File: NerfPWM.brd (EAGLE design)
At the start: 50.8 x 25.4 mm, 37 parts, among them IC1 MEGA48/88/168-AU

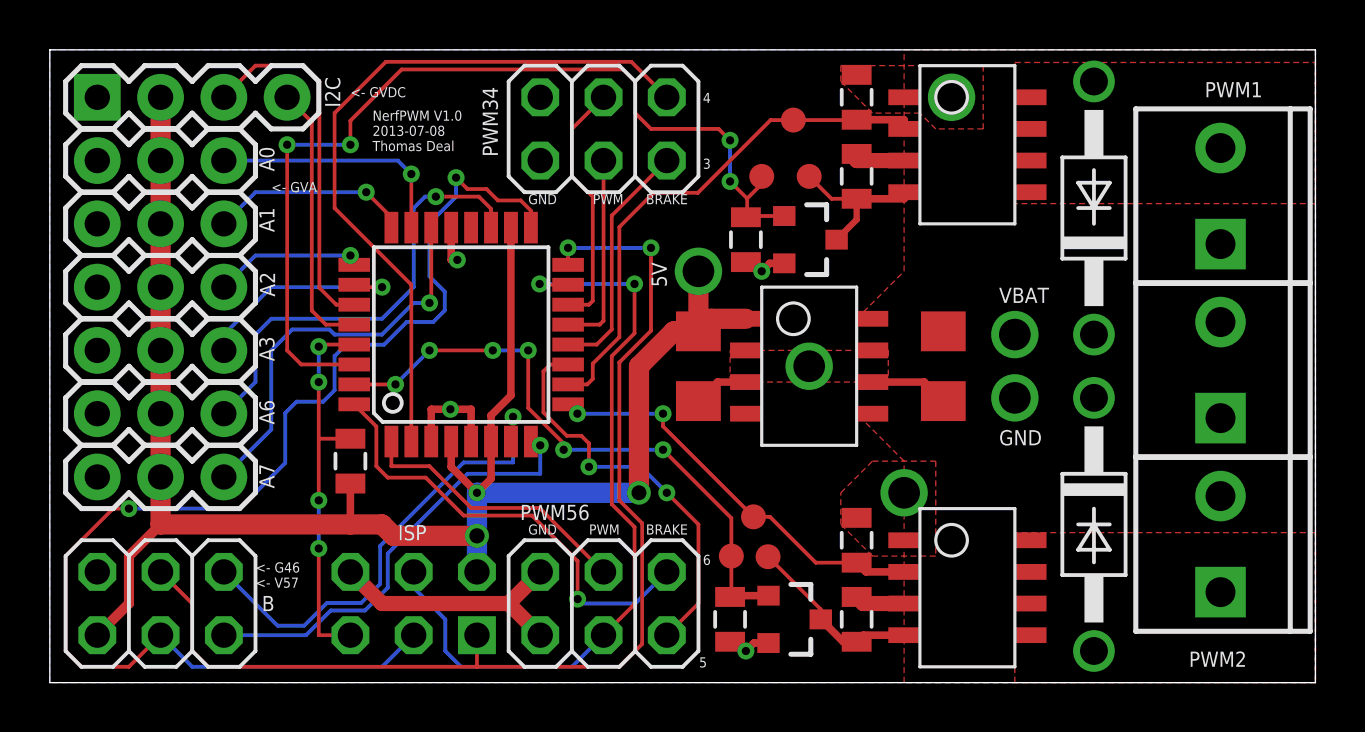
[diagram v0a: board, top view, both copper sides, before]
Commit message: Changed ISP header.
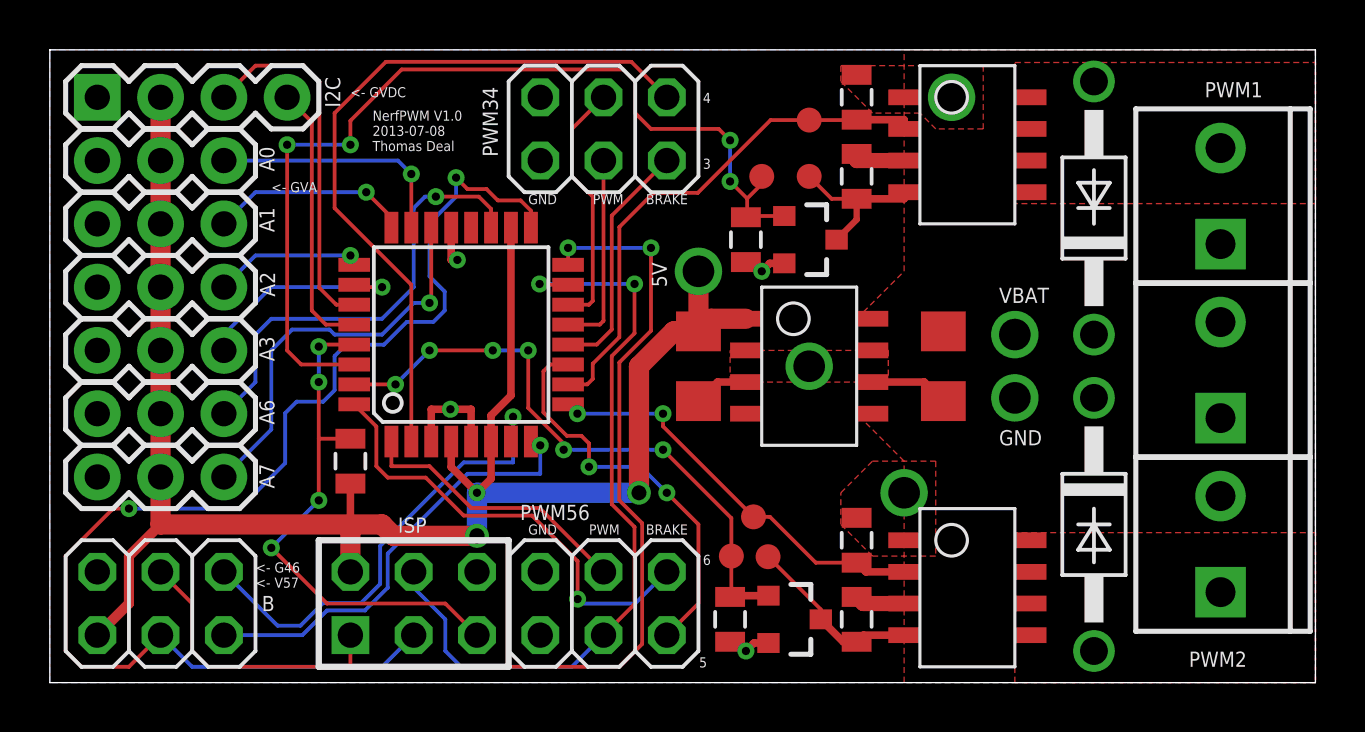
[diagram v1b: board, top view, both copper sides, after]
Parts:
- JP1: value AVR-ISP-6R -> AVR-ISP-6; device custom:AVR-ISP-6R -> custom:AVR-ISP-6
- moved PWM1 0.64 mm to (30.5, 22.6)
- flipped JP1 to the top
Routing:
- net GND: track 25.2 -> 14.8 mm
- net RESET: track 15.6 -> 21.3 mm
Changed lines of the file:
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@@
 <text x="26.0604" y="0.6096" size="0.4064" layer="21">5</text>
 <text x="26.2128" y="4.7244" size="0.4064" layer="21">6</text>
-<text x="13.97" y="5.715" size="0.6096" layer="21">ISP</text>
+<text x="13.97" y="6.0198" size="0.6096" layer="21">ISP</text>
 <text x="8.89" y="19.685" size="0.4064" layer="21">&lt;- GVA</text>
 <text x="12.065" y="23.495" size="0.4064" layer="21">&lt;- GVDC</text>
@@
 <attribute name="VALUE" x="29.6545" y="3.556" size="0.4064" layer="27" rot="R270"/>
 </element>
-<element name="JP1" library="custom" package="AVR-ISP-6R" value="AVR-ISP-6R" x="14.605" y="3.175" smashed="yes" rot="MR0"/>
+<element name="JP1" library="custom" package="AVR-ISP-6" value="AVR-ISP-6" x="14.605" y="3.175" smashed="yes"/>
 <element name="I2C" library="SparkFun" package="1X04" value="" x="1.905" y="23.495" smashed="yes">
 <attribute name="NAME" x="11.049" y="24.3078" size="0.6096" layer="21" ratio="10" rot="R270"/>
@@
 <attribute name="TP_SIGNAL_NAME" value="" x="28.2448" y="4.7498" size="1" layer="37"/>
 </element>
-<element name="PWM1" library="testpad" package="TP10R" value="TPTP10R" x="29.845" y="22.5806" smashed="yes">
-<attribute name="TP_SIGNAL_NAME" value="" x="29.845" y="20.6756" size="1" layer="37"/>
+<element name="PWM1" library="testpad" package="TP10R" value="TPTP10R" x="30.48" y="22.5806" smashed="yes">
+<attribute name="TP_SIGNAL_NAME" value="" x="30.48" y="20.6756" size="1" layer="37"/>
 </element>
 <element name="BRAKE1" library="testpad" package="TP10R" value="TPTP10R" x="28.575" y="20.32" smashed="yes">
@@
 <wire x1="27.305" y1="1.64" x2="27.57" y2="1.64" width="0.3048" layer="1"/>
 <wire x1="27.57" y1="1.64" x2="27.94" y2="1.27" width="0.3048" layer="1"/>
-<wire x1="19.685" y1="4.445" x2="18.415" y2="3.175" width="0.6096" layer="1"/>
-<wire x1="18.415" y1="3.175" x2="19.685" y2="1.905" width="0.6096" layer="1"/>
-<wire x1="18.415" y1="3.175" x2="13.335" y2="3.175" width="0.6096" layer="1"/>
-<wire x1="13.335" y1="3.175" x2="12.065" y2="4.445" width="0.6096" layer="1"/>
 <via x="38.735" y="11.43" extent="1-16" drill="1.27"/>
 </signal>
@@
 <wire x1="26.035" y1="14.1" x2="26.54" y2="14.605" width="0.8128" layer="1"/>
 <wire x1="26.54" y1="14.605" x2="27.94" y2="14.605" width="0.8128" layer="1"/>
-<wire x1="17.145" y1="4.445" x2="17.145" y2="5.8928" width="0.8128" layer="16"/>
 <via x="17.145" y="5.8928" extent="1-16" drill="0.6096"/>
 <wire x1="1.905" y1="1.905" x2="3.175" y2="3.175" width="0.4064" layer="1"/>
@@
 <via x="26.035" y="16.51" extent="1-16" drill="1.27"/>
 <wire x1="26.035" y1="16.51" x2="26.035" y2="14.1" width="0.8128" layer="1"/>
+<wire x1="12.065" y1="6.35" x2="12.065" y2="4.445" width="0.8128" layer="1"/>
 </signal>
 <signal name="VMOT1" class="3">
@@
 <contactref element="PWM1" pad="TP"/>
 <wire x1="32.385" y1="22.595" x2="32.3706" y2="22.5806" width="0.1524" layer="1"/>
-<wire x1="32.3706" y1="22.5806" x2="29.845" y2="22.5806" width="0.1524" layer="1"/>
-<wire x1="29.845" y1="22.5806" x2="28.9306" y2="22.5806" width="0.1524" layer="1"/>
+<wire x1="32.3706" y1="22.5806" x2="30.48" y2="22.5806" width="0.1524" layer="1"/>
+<wire x1="30.48" y1="22.5806" x2="28.9306" y2="22.5806" width="0.1524" layer="1"/>
 </signal>
 <signal name="BRAKE1">
@@
 <wire x1="4.445" y1="1.905" x2="5.715" y2="0.635" width="0.1524" layer="16"/>
 <wire x1="5.715" y1="0.635" x2="13.335" y2="0.635" width="0.1524" layer="16"/>
-<wire x1="13.335" y1="0.635" x2="14.605" y2="1.905" width="0.1524" layer="16"/>
 <wire x1="19.31" y1="18.2626" x2="19.31" y2="18.9424" width="0.1524" layer="1"/>
 <wire x1="19.31" y1="18.9424" x2="18.8976" y2="19.3548" width="0.1524" layer="1"/>
@@
 <wire x1="1.27" y1="0.635" x2="3.175" y2="0.635" width="0.1524" layer="1"/>
 <wire x1="3.175" y1="0.635" x2="4.445" y2="1.905" width="0.1524" layer="1"/>
+<wire x1="14.605" y1="1.905" x2="13.335" y2="0.635" width="0.1524" layer="16"/>
 </signal>
 <signal name="PWM5">
@@
 <contactref element="IC1" pad="15"/>
 <contactref element="PWM56" pad="3"/>
-<wire x1="14.605" y1="4.445" x2="14.605" y2="3.81" width="0.1524" layer="16"/>
-<wire x1="14.605" y1="3.81" x2="15.875" y2="2.54" width="0.1524" layer="16"/>
-<wire x1="15.875" y1="2.54" x2="15.875" y2="1.27" width="0.1524" layer="16"/>
-<wire x1="15.875" y1="1.27" x2="16.51" y2="0.635" width="0.1524" layer="16"/>
 <wire x1="16.51" y1="0.635" x2="20.955" y2="0.635" width="0.1524" layer="16"/>
 <wire x1="20.955" y1="0.635" x2="22.225" y2="1.905" width="0.1524" layer="16"/>
@@
 <wire x1="23.4696" y1="6.2484" x2="23.4696" y2="3.1496" width="0.1524" layer="1"/>
 <wire x1="23.4696" y1="3.1496" x2="22.225" y2="1.905" width="0.1524" layer="1"/>
+<wire x1="14.605" y1="4.445" x2="14.605" y2="3.81" width="0.1524" layer="16"/>
+<wire x1="14.605" y1="3.81" x2="15.875" y2="2.54" width="0.1524" layer="16"/>
+<wire x1="15.875" y1="2.54" x2="15.875" y2="1.27" width="0.1524" layer="16"/>
+<wire x1="15.875" y1="1.27" x2="16.51" y2="0.635" width="0.1524" layer="16"/>
 </signal>
 <signal name="B4">
@@
 <wire x1="5.715" y1="3.175" x2="5.715" y2="1.27" width="0.1524" layer="1"/>
 <wire x1="5.715" y1="1.27" x2="6.35" y2="0.635" width="0.1524" layer="1"/>
-<wire x1="6.35" y1="0.635" x2="17.145" y2="0.635" width="0.1524" layer="1"/>
-<wire x1="17.145" y1="0.635" x2="22.86" y2="0.635" width="0.1524" layer="1"/>
+<wire x1="6.35" y1="0.635" x2="12.065" y2="0.635" width="0.1524" layer="1"/>
+<wire x1="12.065" y1="0.635" x2="22.86" y2="0.635" width="0.1524" layer="1"/>
 <wire x1="22.86" y1="7.3152" x2="22.86" y2="12.8524" width="0.1524" layer="1"/>
 <wire x1="22.86" y1="12.8524" x2="24.13" y2="14.1224" width="0.1524" layer="1"/>
@@
 <wire x1="23.7744" y1="6.4008" x2="23.7744" y2="1.5494" width="0.1524" layer="1"/>
 <wire x1="23.7744" y1="1.5494" x2="22.86" y2="0.635" width="0.1524" layer="1"/>
-<wire x1="17.145" y1="1.905" x2="17.145" y2="0.635" width="0.1524" layer="1"/>
+<wire x1="12.065" y1="1.905" x2="12.065" y2="0.635" width="0.1524" layer="1"/>
 </signal>
 <signal name="RESET">
@@
 <wire x1="10.795" y1="12.065" x2="10.795" y2="9.79" width="0.1524" layer="1"/>
 <wire x1="10.795" y1="9.79" x2="12.065" y2="9.79" width="0.1524" layer="1"/>
-<wire x1="12.065" y1="1.905" x2="10.795" y2="1.905" width="0.1524" layer="1"/>
-<wire x1="10.795" y1="1.905" x2="10.795" y2="5.3848" width="0.1524" layer="1"/>
-<via x="10.795" y="5.3848" extent="1-16" drill="0.3302"/>
-<wire x1="10.795" y1="5.3848" x2="10.795" y2="7.3152" width="0.1524" layer="16"/>
+<via x="8.89" y="5.4102" extent="1-16" drill="0.3302"/>
+<wire x1="8.89" y1="5.4102" x2="10.795" y2="7.3152" width="0.1524" layer="16"/>
 <via x="10.795" y="7.3152" extent="1-16" drill="0.3302"/>
 <wire x1="10.795" y1="7.3152" x2="10.795" y2="9.79" width="0.1524" layer="1"/>
+<wire x1="11.1252" y1="3.175" x2="15.875" y2="3.175" width="0.1524" layer="1"/>
+<wire x1="15.875" y1="3.175" x2="17.145" y2="1.905" width="0.1524" layer="1"/>
+<wire x1="11.1252" y1="3.175" x2="8.89" y2="5.4102" width="0.1524" layer="1"/>
 </signal>
 <signal name="SDA">
@@
 <wire x1="13.5636" y1="5.1816" x2="13.5636" y2="3.81" width="0.1524" layer="16"/>
 <wire x1="13.5636" y1="3.81" x2="12.6492" y2="2.8956" width="0.1524" layer="16"/>
-<wire x1="12.6492" y1="2.8956" x2="11.2776" y2="2.8956" width="0.1524" layer="16"/>
-<wire x1="11.2776" y1="2.8956" x2="10.287" y2="1.905" width="0.1524" layer="16"/>
-<wire x1="10.287" y1="1.905" x2="6.985" y2="1.905" width="0.1524" layer="16"/>
+<wire x1="12.6492" y1="2.8956" x2="11.1252" y2="2.8956" width="0.1524" layer="16"/>
+<wire x1="11.1252" y1="2.8956" x2="10.1346" y2="1.905" width="0.1524" layer="16"/>
+<wire x1="10.1346" y1="1.905" x2="6.985" y2="1.905" width="0.1524" layer="16"/>
 </signal>
 <signal name="B6">
@@
 <wire x1="13.2588" y1="5.4864" x2="13.2588" y2="3.9624" width="0.1524" layer="16"/>
 <wire x1="13.2588" y1="3.9624" x2="12.4968" y2="3.2004" width="0.1524" layer="16"/>
-<wire x1="12.4968" y1="3.2004" x2="11.1252" y2="3.2004" width="0.1524" layer="16"/>
-<wire x1="11.1252" y1="3.2004" x2="10.2108" y2="2.286" width="0.1524" layer="16"/>
+<wire x1="12.4968" y1="3.2004" x2="10.9728" y2="3.2004" width="0.1524" layer="16"/>
+<wire x1="10.9728" y1="3.2004" x2="10.0584" y2="2.286" width="0.1524" layer="16"/>
 <wire x1="9.144" y1="2.286" x2="6.985" y2="4.445" width="0.1524" layer="16"/>
-<wire x1="10.2108" y1="2.286" x2="9.144" y2="2.286" width="0.1524" layer="16"/>
+<wire x1="10.0584" y1="2.286" x2="9.144" y2="2.286" width="0.1524" layer="16"/>
 </signal>
 </signals>
